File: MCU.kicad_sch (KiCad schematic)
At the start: 21 parts, among them U3 M95256-RDW6TP, U4 STM32G474RETx, U5 TCAN1044V-Q1

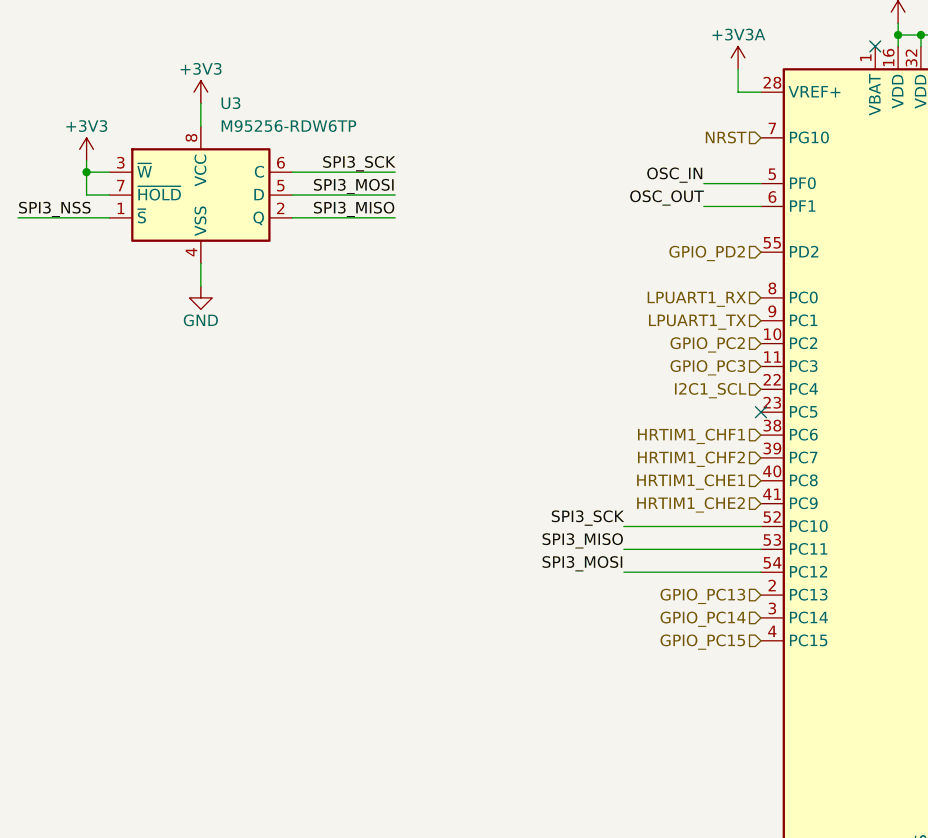
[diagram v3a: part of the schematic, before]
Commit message: Figured out GPIO and added oscillator to schematic, need to pick part
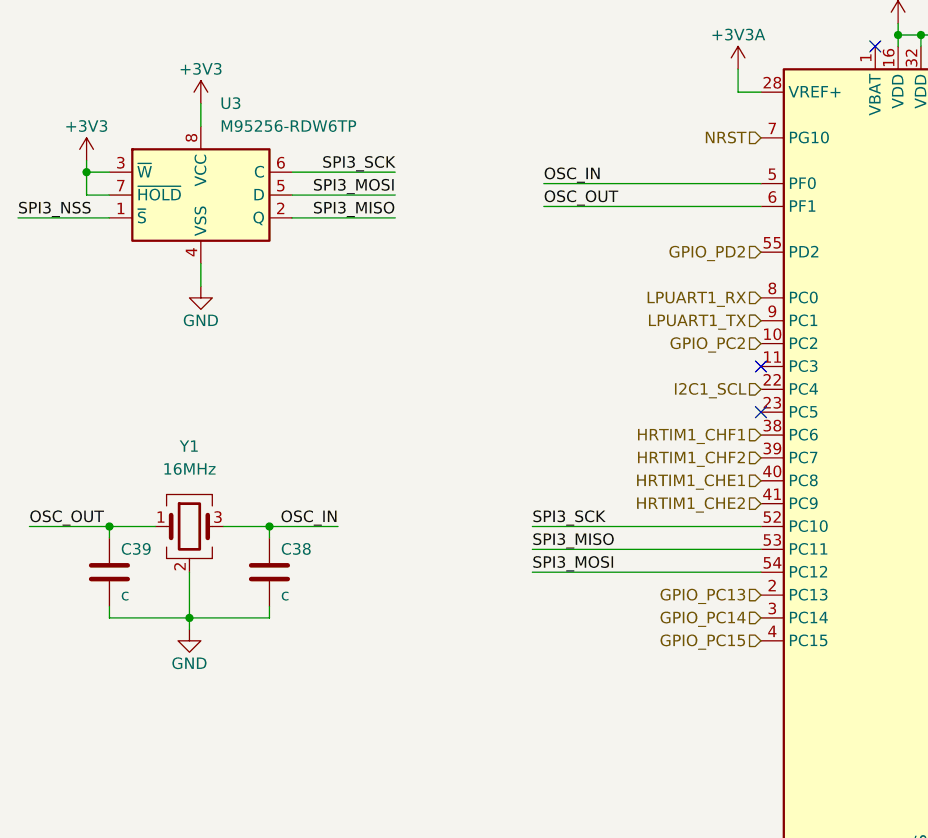
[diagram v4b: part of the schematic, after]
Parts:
- added C38, C39: c, Capacitor_SMD:C_0402_1005Metric, symbol Device:C
- added Y1: 16MHz, symbol Device:Crystal_GND24
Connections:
- net GND: now also C38.2, C39.2, Y1.2 (G), Y1.4 (G)
- net OSC_IN: now also C38.1, Y1.3
- net OSC_OUT: now also C39.1, Y1.1
- net GPIO_PC3: no longer names the net of U4.11 (PC3)
- no-connect marks 5 -> 6

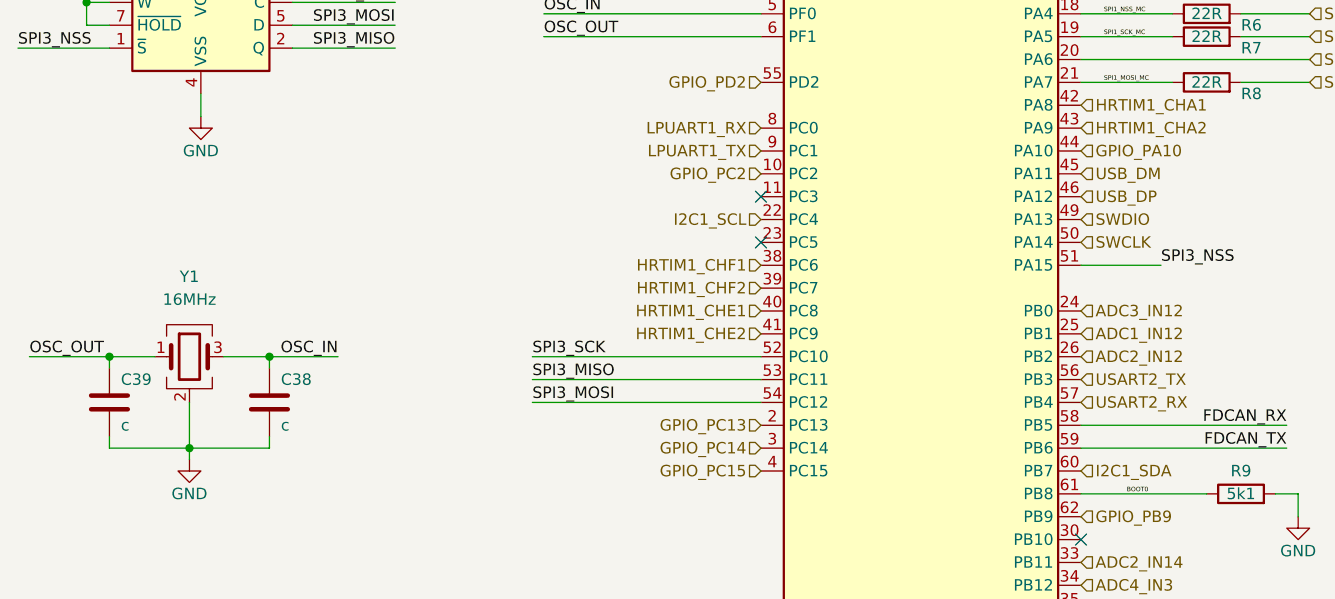
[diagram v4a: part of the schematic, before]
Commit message: Moved MCU to make more room for routing, updated crystal package/PN
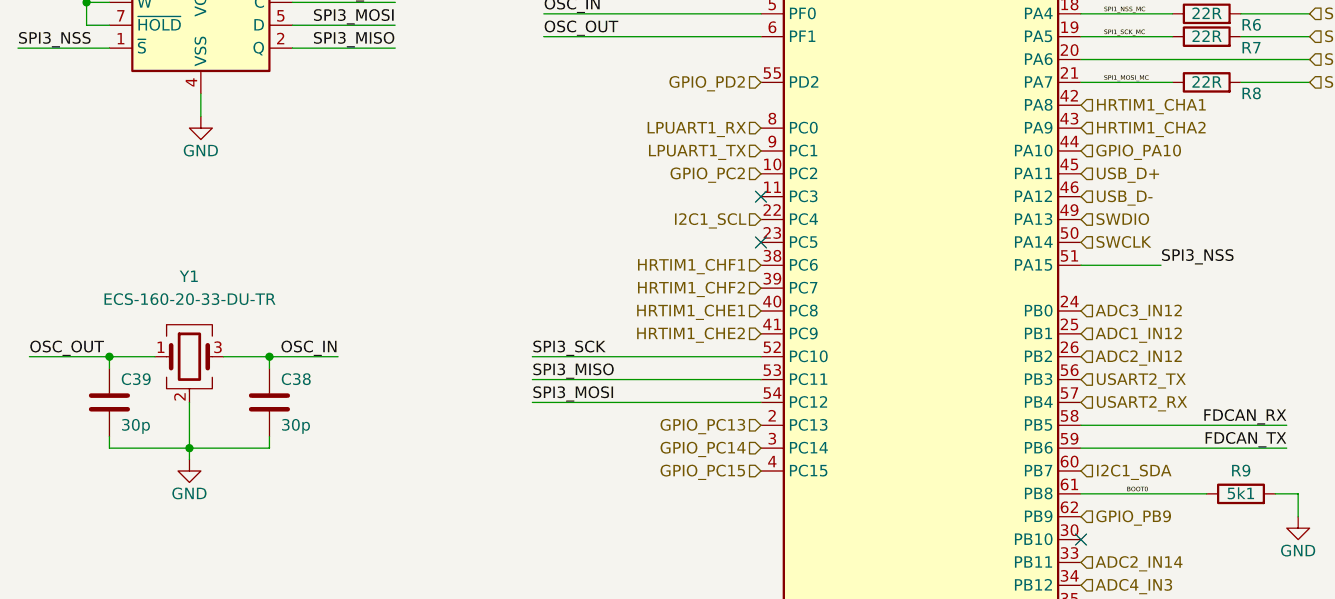
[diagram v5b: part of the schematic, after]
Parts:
- C38, C39: value c -> 30p
- Y1: value 16MHz -> ECS-160-20-33-DU-TR; footprint (none) -> Oscillator:Oscillator_SMD_Abracon_ASE-4Pin_3.2x2.5mm
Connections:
- net USB_DM renamed USB_D+
- net USB_DP renamed USB_D-
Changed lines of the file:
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@@
 		)
 	)
-	(hierarchical_label "USB_DP"
+	(hierarchical_label "USB_D-"
 		(shape input)
 		(at 158.75 97.79 0)
@@
 		)
 	)
-	(hierarchical_label "USB_DM"
+	(hierarchical_label "USB_D+"
 		(shape input)
 		(at 158.75 95.25 0)
@@
 			)
 		)
-		(property "Value" "c"
+		(property "Value" "30p"
 			(at 52.07 123.19 0)
 			(effects
@@
 			)
 		)
-		(property "Value" "16MHz"
+		(property "Value" "ECS-160-20-33-DU-TR"
 			(at 59.69 109.22 0)
 			(effects
@@
 			)
 		)
-		(property "Footprint" ""
+		(property "Footprint" "Oscillator:Oscillator_SMD_Abracon_ASE-4Pin_3.2x2.5mm"
 			(at 59.69 115.57 0)
 			(effects
@@
 			)
 		)
-		(property "Datasheet" "~"
+		(property "Datasheet" "https://ecsxtal.com/store/pdf/ecx-32.pdf"
 			(at 59.69 115.57 0)
 			(effects
@@
 			)
 		)
-		(property "Description" "Four pin crystal, GND on pins 2 and 4"
+		(property "Description" "16MHz Four pin crystal, GND on pins 2 and 4"
 			(at 59.69 115.57 0)
 			(effects
@@
 			)
 		)
-		(property "Value" "c"
+		(property "Value" "30p"
 			(at 69.85 123.19 0)
 			(effects

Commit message: Routing
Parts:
- U5: footprint Package_SO:SOIC-8_3.9x4.9mm_P1.27mm -> Package_TO_SOT_SMD:TSOT-23-8
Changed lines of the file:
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@@
 			)
 		)
-		(property "Footprint" "Package_SO:SOIC-8_3.9x4.9mm_P1.27mm"
+		(property "Footprint" "Package_TO_SOT_SMD:TSOT-23-8"
 			(at 223.52 140.97 0)
 			(effects

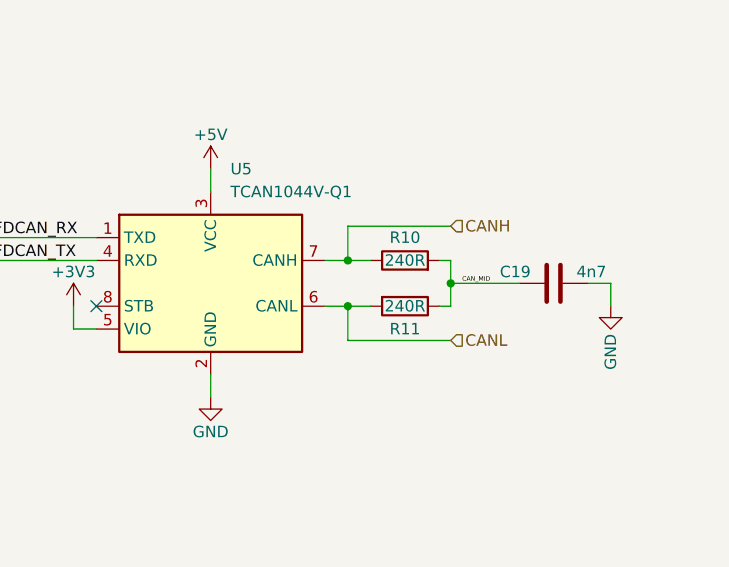
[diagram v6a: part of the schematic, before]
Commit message: Adjusted cap sizes, 0603 for all need hand soldering, 0402 where possible, 0804 as needed
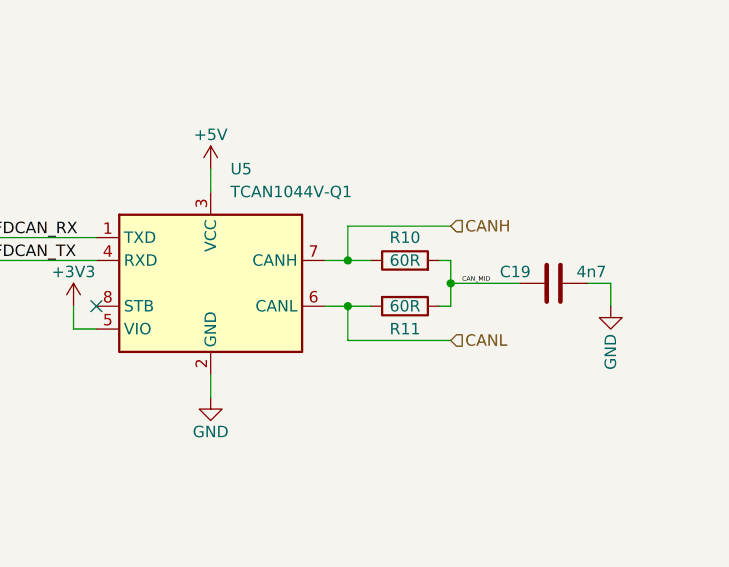
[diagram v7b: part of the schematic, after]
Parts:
- C14, C17, C9: footprint Capacitor_SMD:C_0402_1005Metric -> Capacitor_SMD:C_0603_1608Metric
- R10, R11: value 240R -> 60R; footprint Resistor_SMD:R_0402_1005Metric -> Resistor_SMD:R_0603_1608Metric
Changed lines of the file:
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@@
 			)
 		)
-		(property "Footprint" "Capacitor_SMD:C_0402_1005Metric"
+		(property "Footprint" "Capacitor_SMD:C_0603_1608Metric"
 			(at 155.9052 35.56 0)
 			(effects
@@
 			)
 		)
-		(property "Value" "240R"
+		(property "Value" "60R"
 			(at 245.11 125.73 90)
 			(effects
@@
 			)
 		)
-		(property "Footprint" "Resistor_SMD:R_0402_1005Metric"
+		(property "Footprint" "Resistor_SMD:R_0603_1608Metric"
 			(at 245.11 127.508 90)
 			(effects
@@
 			)
 		)
-		(property "Value" "240R"
+		(property "Value" "60R"
 			(at 245.11 130.81 90)
 			(effects
@@
 			)
 		)
-		(property "Footprint" "Resistor_SMD:R_0402_1005Metric"
+		(property "Footprint" "Resistor_SMD:R_0603_1608Metric"
 			(at 245.11 129.032 90)
 			(effects
@@
 			)
 		)
-		(property "Footprint" "Capacitor_SMD:C_0402_1005Metric"
+		(property "Footprint" "Capacitor_SMD:C_0603_1608Metric"
 			(at 107.6452 35.56 0)
 			(effects
@@
 			)
 		)
-		(property "Footprint" "Capacitor_SMD:C_0402_1005Metric"
+		(property "Footprint" "Capacitor_SMD:C_0603_1608Metric"
 			(at 248.6152 35.56 0)
 			(effects

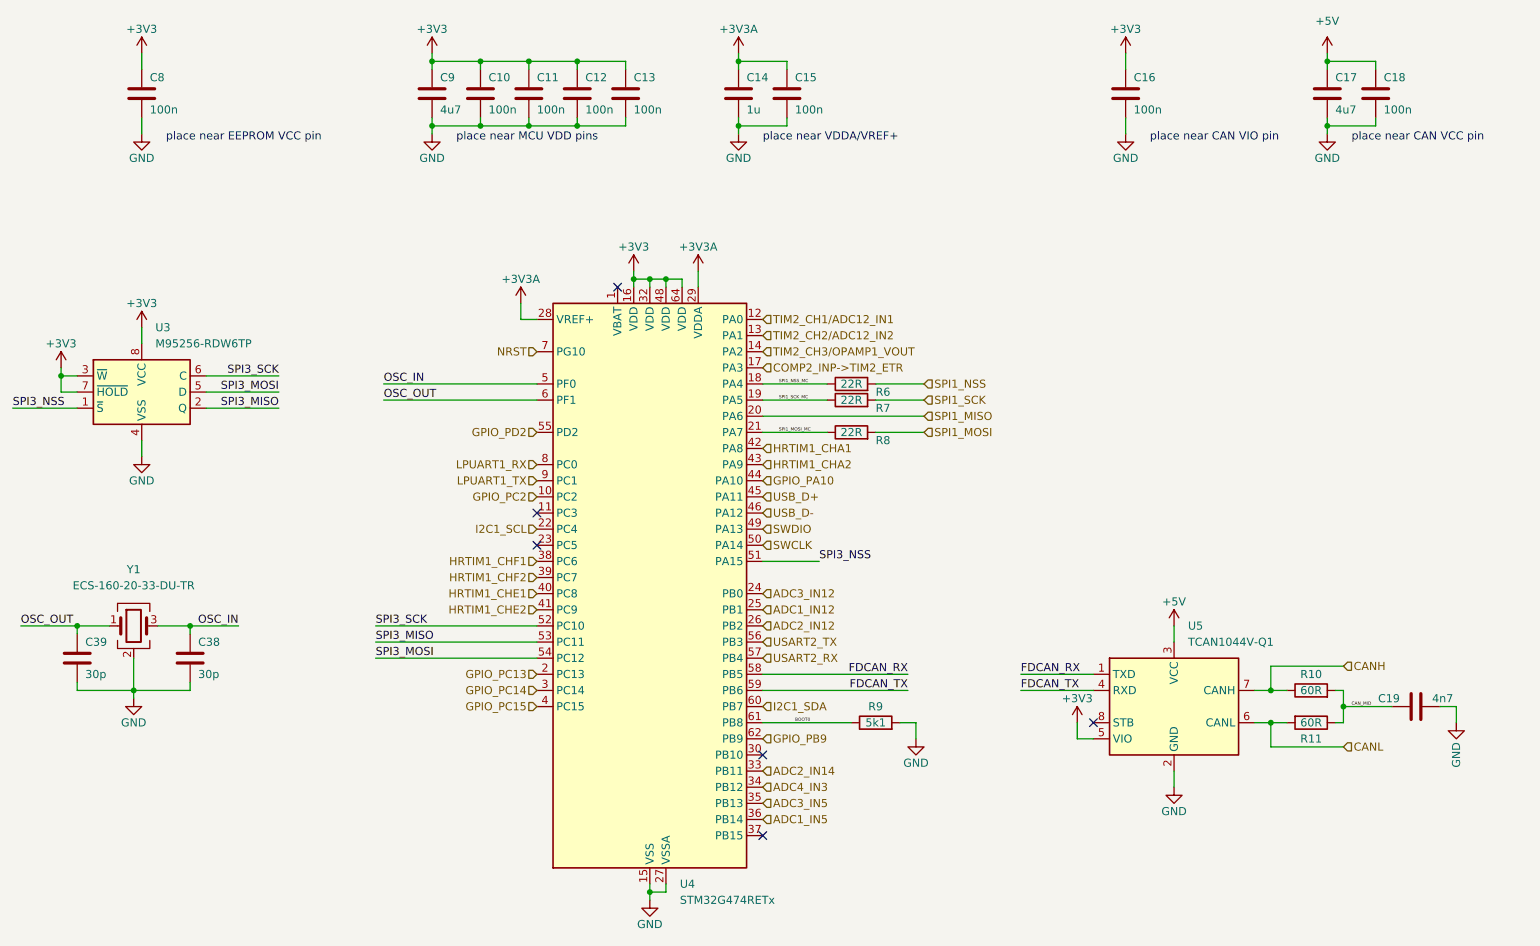
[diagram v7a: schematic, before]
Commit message: Updating all decoupling to 1u
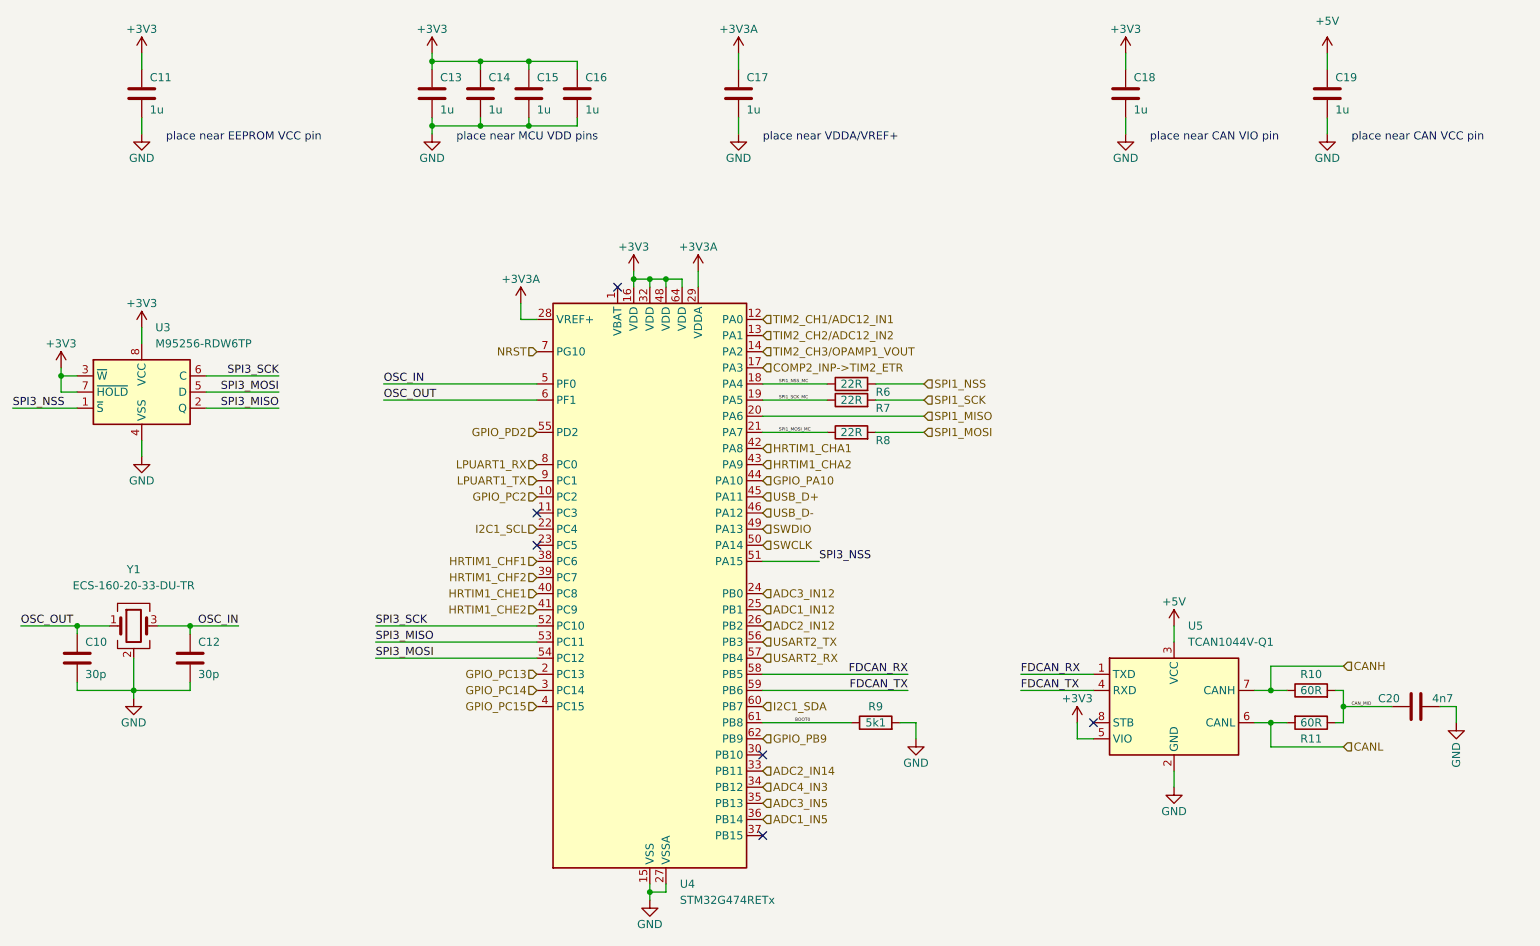
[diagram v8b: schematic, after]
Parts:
- removed C15: 100n, Capacitor_SMD:C_0402_1005Metric, symbol Device:C
- removed C17, C9: 4u7, Capacitor_SMD:C_0603_1608Metric, symbol Device:C
- C11: renamed from C8; value 100n -> 1u
- C13: renamed from C10; value 100n -> 1u
- C14: renamed from C11; value 100n -> 1u
- C15: renamed from C12; value 100n -> 1u
- C16: renamed from C13; value 100n -> 1u
- C17: renamed from C14; footprint Capacitor_SMD:C_0603_1608Metric -> Capacitor_SMD:C_0402_1005Metric
- C18: renamed from C16; value 100n -> 1u
- C19: renamed from C18; value 100n -> 1u
- renumbered C39 to C10, C38 to C12, C19 to C20
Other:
- moved on the sheet: C13, C14, C15, C16, C19
